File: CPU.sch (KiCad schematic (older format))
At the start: 30 parts, among them IC102 z80_6128, IC103 SED9420Cac, IC116 74HCT02, Q101 KTC1815Y

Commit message: more accurate on pins definition, power, centronic 36, jack, and some wiring
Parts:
- R210: footprint (none) -> Resistor_THT:R_Axial_DIN0207_L6.3mm_D2.5mm_P10.16mm_Horizontal
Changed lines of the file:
@@
 F 0 "R210" H 2668 1496 50  0000 L CNN
 F 1 "470k" H 2668 1405 50  0000 L CNN
-F 2 "" H 2600 1450 50  0001 C CNN
+F 2 "Resistor_THT:R_Axial_DIN0207_L6.3mm_D2.5mm_P10.16mm_Horizontal" H 2600 1450 50  0001 C CNN
 F 3 "~" H 2600 1450 50  0001 C CNN
 	1    2600 1450

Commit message: finished the centronic 36, some more refinements on placement, new footprint for some connectors
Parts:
- CP101, CP102: footprint Connector_PinSocket_2.00mm:PinSocket_2x09_P2.00mm_Vertical -> cpc6128+:CP01_02
- CP107: footprint Connector_PinHeader_1.00mm:PinHeader_1x08_P1.00mm_Vertical -> cpc6128+:CP_107
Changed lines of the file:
@@
 F 0 "CP101" V 8315 880 50  0000 C CNN
 F 1 "5242-18CHPB" V 8224 880 50  0000 C CNN
-F 2 "Connector_PinSocket_2.00mm:PinSocket_2x09_P2.00mm_Vertical" H 8150 950 50  0001 C CNN
+F 2 "cpc6128+:CP01_02" H 8150 950 50  0001 C CNN
 F 3 "~" H 8150 950 50  0001 C CNN
 	1    8150 950
@@
 F 0 "CP102" V 10365 880 50  0000 C CNN
 F 1 "5242-18CHPB" V 10274 880 50  0000 C CNN
-F 2 "Connector_PinSocket_2.00mm:PinSocket_2x09_P2.00mm_Vertical" H 10200 950 50  0001 C CNN
+F 2 "cpc6128+:CP01_02" H 10200 950 50  0001 C CNN
 F 3 "~" H 10200 950 50  0001 C CNN
 	1    10200 950
@@
 F 0 "CP107" H 6758 1867 50  0000 C CNN
 F 1 "172681-8" H 6758 1776 50  0000 C CNN
-F 2 "Connector_PinHeader_1.00mm:PinHeader_1x08_P1.00mm_Vertical" H 6650 2400 50  0001 C CNN
+F 2 "cpc6128+:CP_107" H 6650 2400 50  0001 C CNN
 F 3 "~" H 6650 2400 50  0001 C CNN
 	1    6650 2400

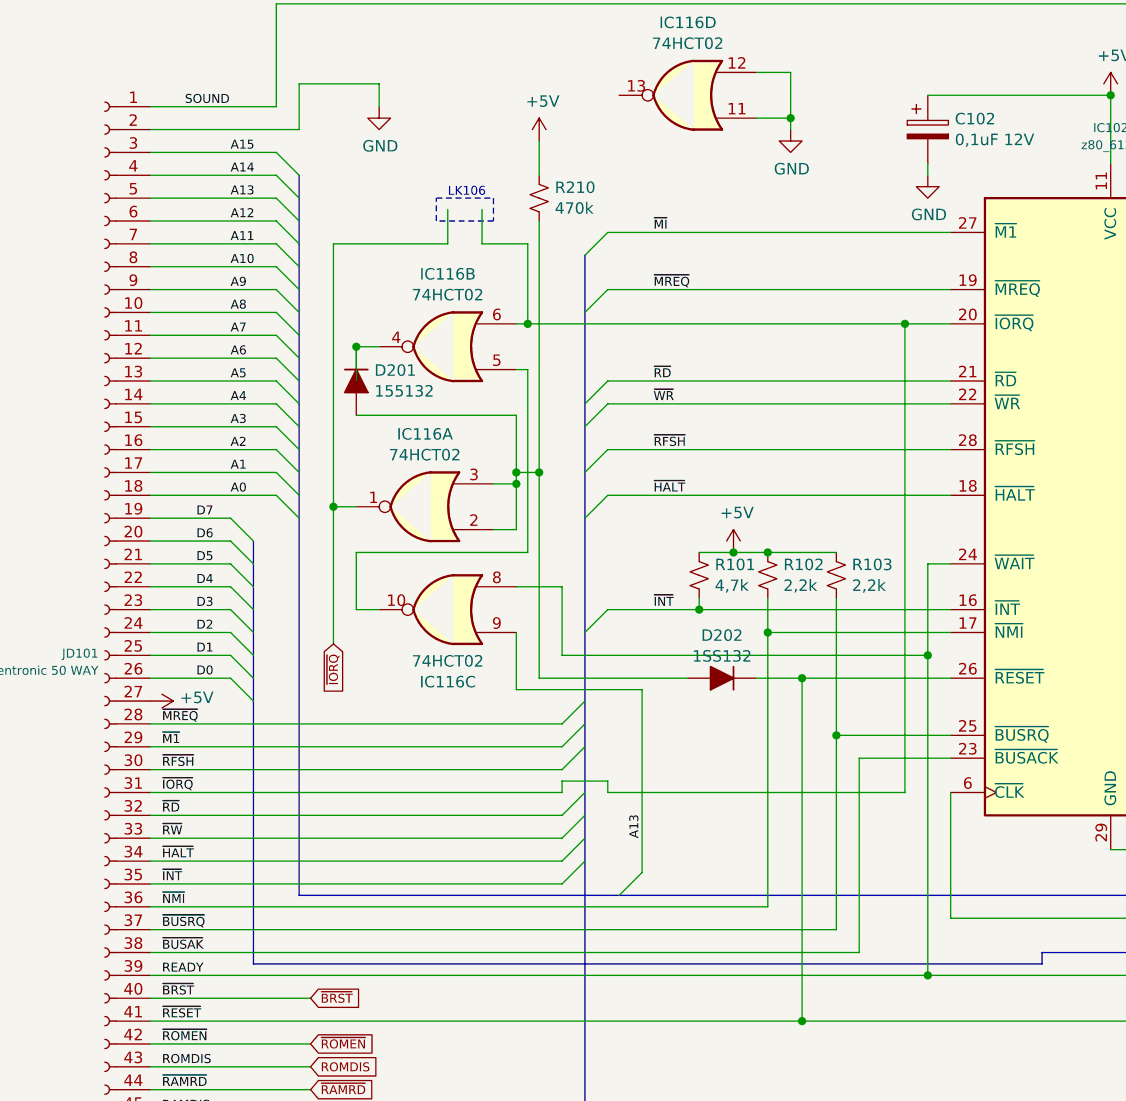
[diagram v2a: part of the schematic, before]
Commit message: More work on centronics port.
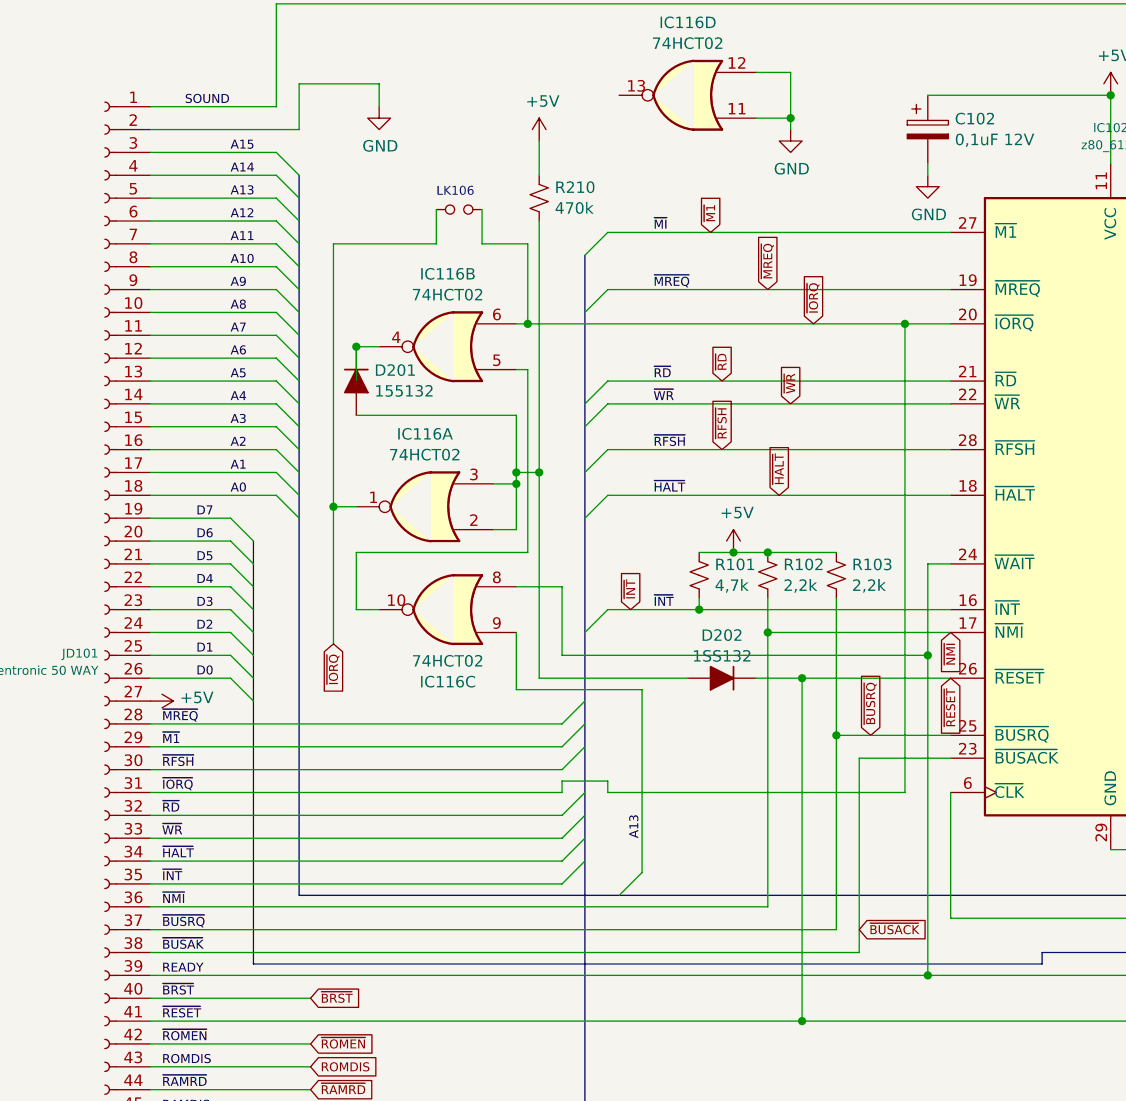
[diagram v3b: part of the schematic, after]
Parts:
- added LK106: Jumper_NO_Small, symbol Device:Jumper_NO_Small
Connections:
- net labels added: ~BUSACK
- net labels removed: ~RW
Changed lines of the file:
@@
 	0    1    1    0
 $EndComp
-Wire Wire Line
-	2200 1500 2200 1650
-Wire Wire Line
-	2200 1650 1700 1650
-Wire Wire Line
-	1700 1650 1700 2800
 Text Label 950  4050 0    39   ~ 0
 ~IORQ
@@
 ~RD
 Text Label 950  4250 0    39   ~ 0
-~RW
+~WR
 Connection ~ 2600 2650
 Wire Wire Line
@@
 Text Label 950  5950 0    39   ~ 0
 CLK4
-Text Notes 2200 1450 0    39   ~ 0
-LK106
-Wire Notes Line
-	2150 1450 2400 1450
-Wire Notes Line
-	2400 1450 2400 1550
-Wire Notes Line
-	2400 1550 2150 1550
-Wire Notes Line
-	2150 1550 2150 1450
 Text GLabel 1700 3400 3    39   Input ~ 0
 ~IORQ
@@
 Text Notes 6300 3450 0    39   ~ 0
 not used\n
+Text GLabel 3600 1850 1    39   Input ~ 0
+~MREQ
+Text GLabel 3400 2250 1    39   Input ~ 0
+~RD
+Text GLabel 3700 2350 1    39   Input ~ 0
+~WR
+Text GLabel 3350 1600 1    39   Input ~ 0
+~M1
+Text GLabel 3000 3250 1    39   Input ~ 0
+~INT
+Text GLabel 3400 2550 1    39   Input ~ 0
+~RFSH
+Text GLabel 3650 2750 1    39   Input ~ 0
+~HALT
+Text GLabel 3800 2000 1    39   Input ~ 0
+~IORQ
+Text GLabel 4000 4650 2    39   Input ~ 0
+~BUSACK
+Text GLabel 4050 3800 1    39   Input ~ 0
+~BUSRQ
+Text GLabel 4400 3550 3    39   Input ~ 0
+~RESET
+Text GLabel 4400 3350 3    39   Input ~ 0
+~NMI
+$Comp
+L Device:Jumper_NO_Small LK106
+U 1 1 6089111E
+P 2250 1500
+F 0 "LK106" H 2250 1593 50  0001 C CNN
+F 1 "Jumper_NO_Small" H 2250 1594 50  0001 C CNN
+F 2 "" H 2250 1500 50  0001 C CNN
+F 3 "~" H 2250 1500 50  0001 C CNN
+	1    2250 1500
+	1    0    0    -1
+$EndComp
+Wire Wire Line
+	1700 1650 2150 1650
 Wire Bus Line
 	1550 4500 6250 4500
@@
 Wire Bus Line
 	6250 1700 6250 4500
+Wire Wire Line
+	1700 1650 1700 2800
+Wire Wire Line
+	2150 1500 2150 1650
+Text Notes 2150 1450 0    39   ~ 0
+LK106
 $EndSCHEMATC
